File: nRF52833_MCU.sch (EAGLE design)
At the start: 44 parts, among them IC1 SKY13415-485LF, J1 282834-2, J100 DEBUG_CONNECTOR, J2 282834-2, J3 282834-2, U1 nRF52833-QIAA, U3 BQ25570RGRR, X1 32MHz, X2 32.768kHz, X3 22-23-2031

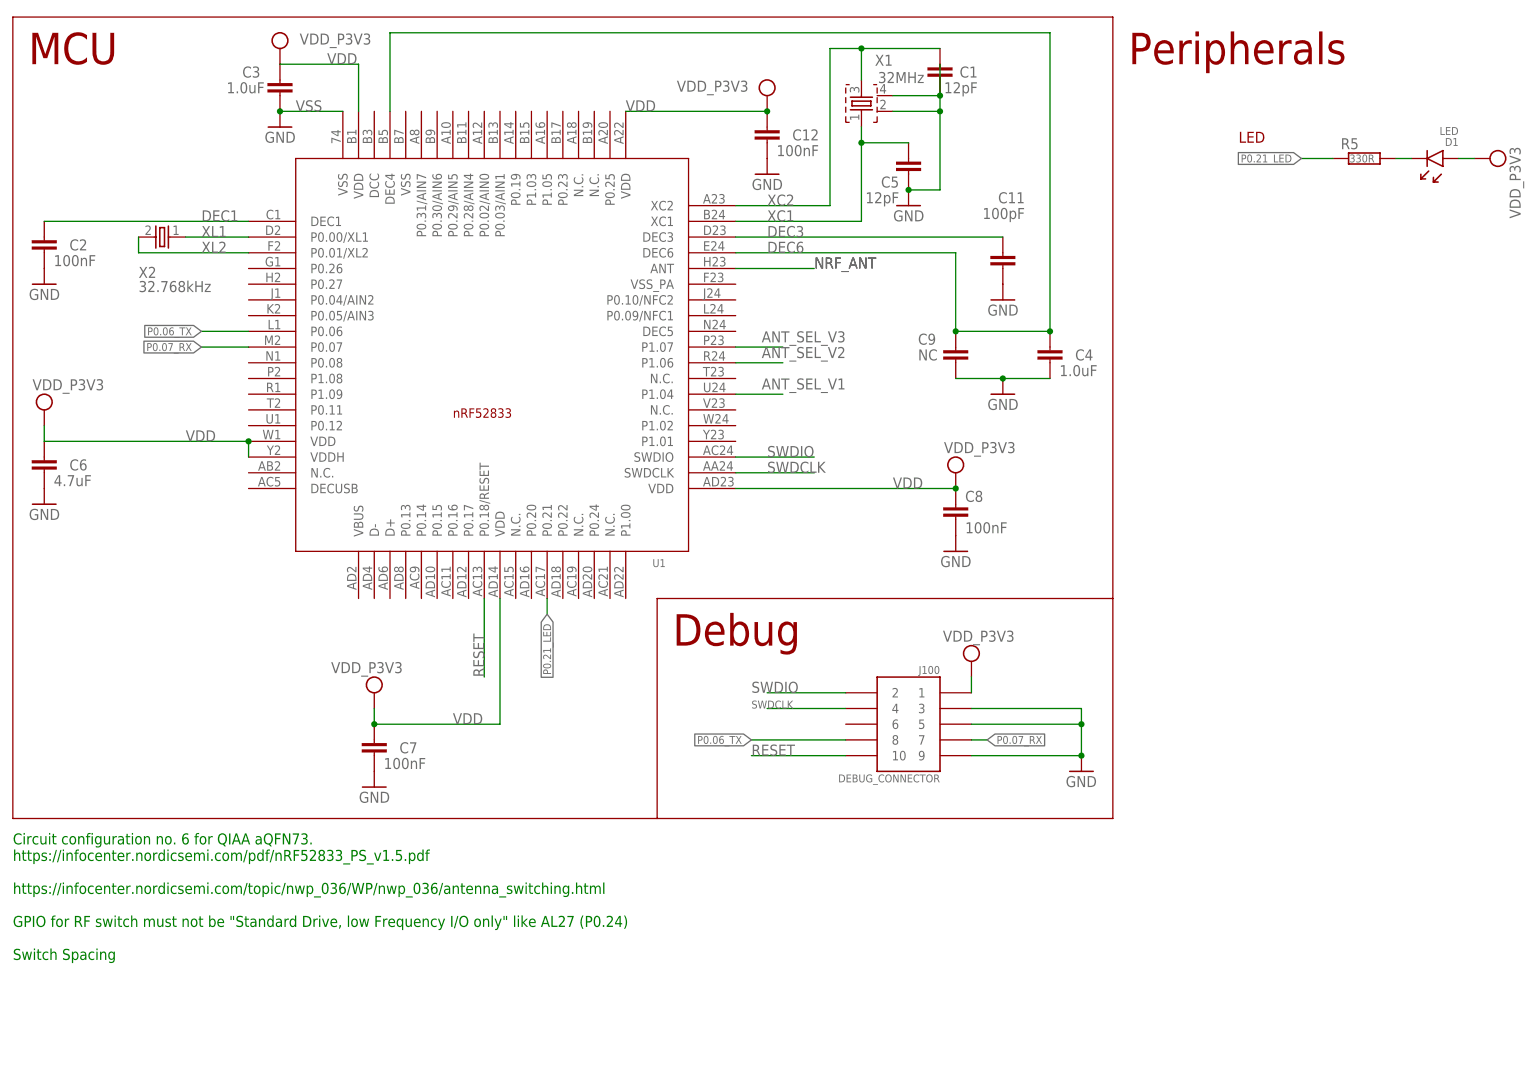
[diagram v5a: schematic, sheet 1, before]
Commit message: Add the 5 antennas
Signed-off-by: Florian Depraz <florian.depraz@outlook.com>
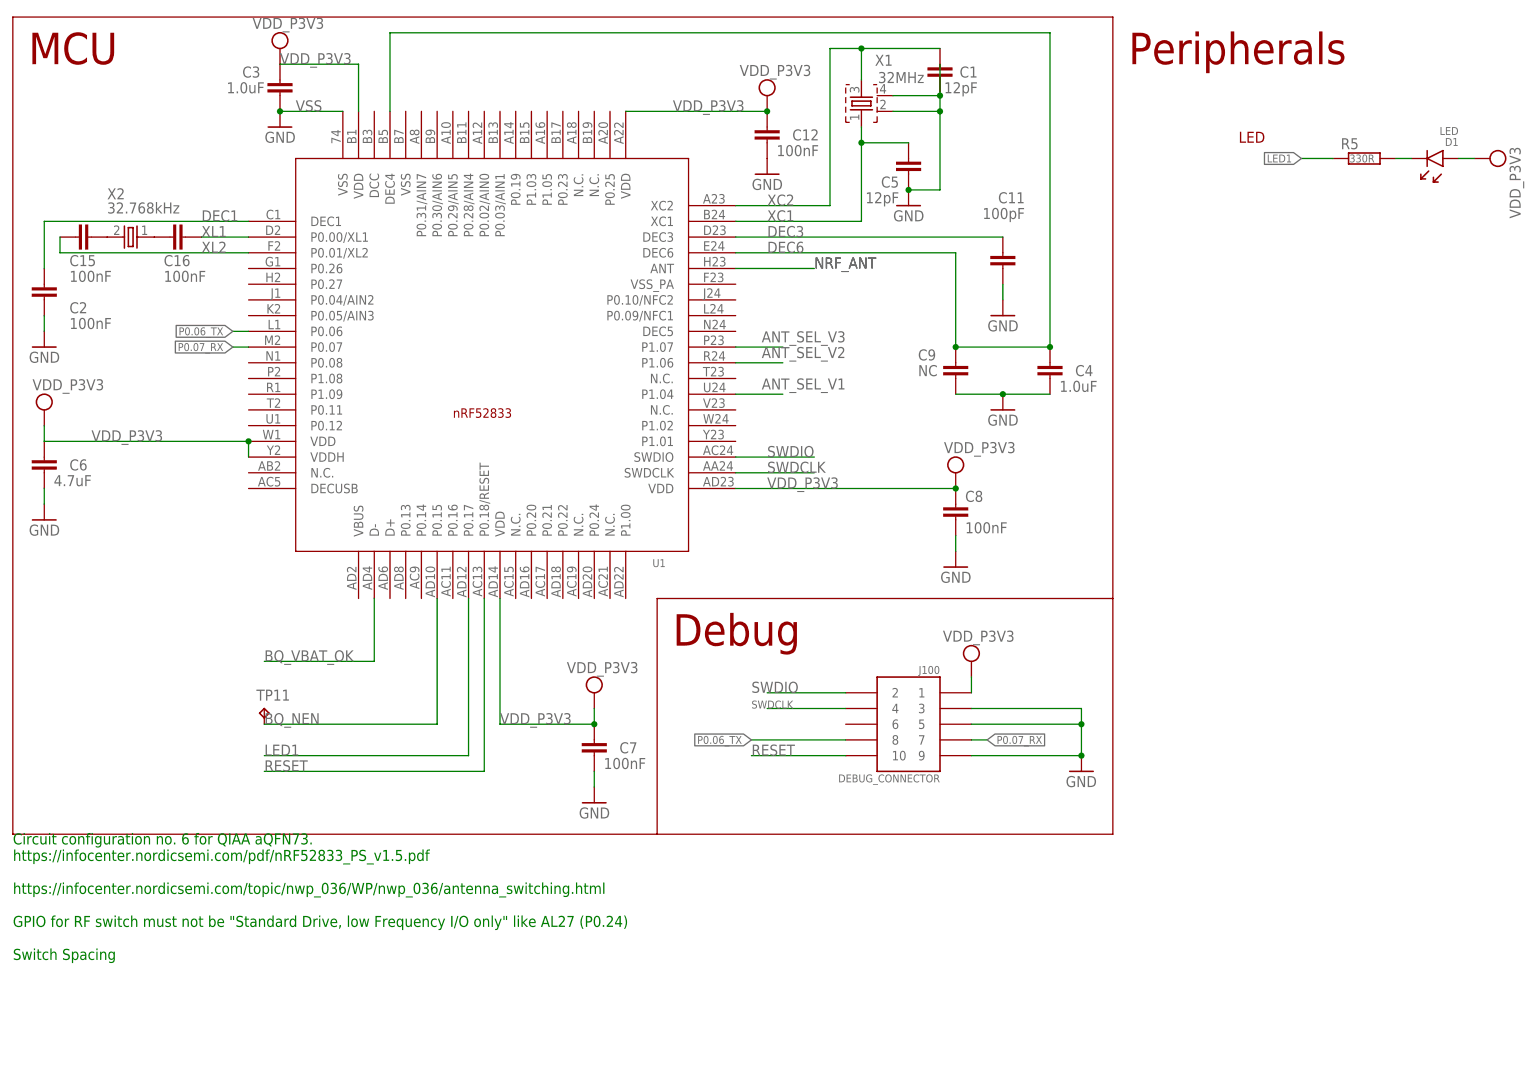
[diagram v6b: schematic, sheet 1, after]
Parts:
- added ANT3: (no value), discrete:ANTENNA
- added ANT4, ANT5: SWRA092B, texas:SWRA092B
- added C15, C16: 100nF, Nordic_misc:CAPACITOR_0402_N
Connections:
- removed net BQ_OK_HYST: U3.OK_HYST
- removed net BQ_OK_PROG: U3.OK_PROG
- removed net GND: C1.2, C10.2, C11.2, C12.2, C13.2, C14.2, C2.2, C20.2, C21.2, C23.2, C24.2, C25.2, C26.2, C27.2, C28.2, C29.2, C4.2, C5.2, C6.2, C7.2, C8.2, C9.2, J1.1, J100.3, J100.5, J100.9, J2.1, J3.1, U3.EP@1, U3.EP@2, U3.EP@3, U3.EP@4, U3.EP@5, U3.NC1, U3.NC2, U3.VSS@1, U3.VSS@2, X1.2, X1.4
- removed net P0.21_LED: R5.1, U1.P0.21
- removed net VDD: C12.1, C3.1, C6.1, C7.1, C8.1, U1.VDD@1, U1.VDD@2, U1.VDD@3, U1.VDD@4, U1.VDD@5, U1.VDDH
- new net LED1: R5.1, U1.P0.17
- new net N$2: C16.2, X2.1
- new net N$3: C15.2, X2.2
- net ANT_OUT_RF3: now also ANT4.ANTENNA
- net ANT_OUT_RF4: now also ANT3.1
- net ANT_OUT_RF5: now also ANT5.ANTENNA
- net BQ_NEN: now also TP11.TP, U1.P0.15
- net BQ_VBAT_OK: now also U1.D-
- net VDD_P3V3: now also C12.1, C3.1, C6.1, C7.1, C8.1, U1.VDD@1, U1.VDD@2, U1.VDD@3, U1.VDD@4, U1.VDD@5, U1.VDDH
- net VSS: now also C1.2, C10.2, C11.2, C12.2, C13.2, C14.2, C2.2, C20.2, C21.2, C23.2, C24.2, C25.2, C26.2, C27.2, C28.2, C29.2, C4.2, C5.2, C6.2, C7.2, C8.2, C9.2, J1.1, J100.3, J100.5, J100.9, J2.1, J3.1, U3.EP@1, U3.EP@2, U3.EP@3, U3.EP@4, U3.EP@5, U3.NC1, U3.NC2, U3.OK_HYST, U3.OK_PROG, U3.VSS@1, U3.VSS@2, X1.2, X1.4
- net XL1: now also C16.1; no longer X2.1
- net XL2: now also C15.1; no longer X2.2
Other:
- moved on the sheet: C2, C4, C7, C9, X2

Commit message: Fix errors
Signed-off-by: Florian Depraz <florian.depraz@outlook.com>
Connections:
- net VDD_P3V3 renamed VDD
- net VSS renamed GND
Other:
- moved on the sheet: C3, C6

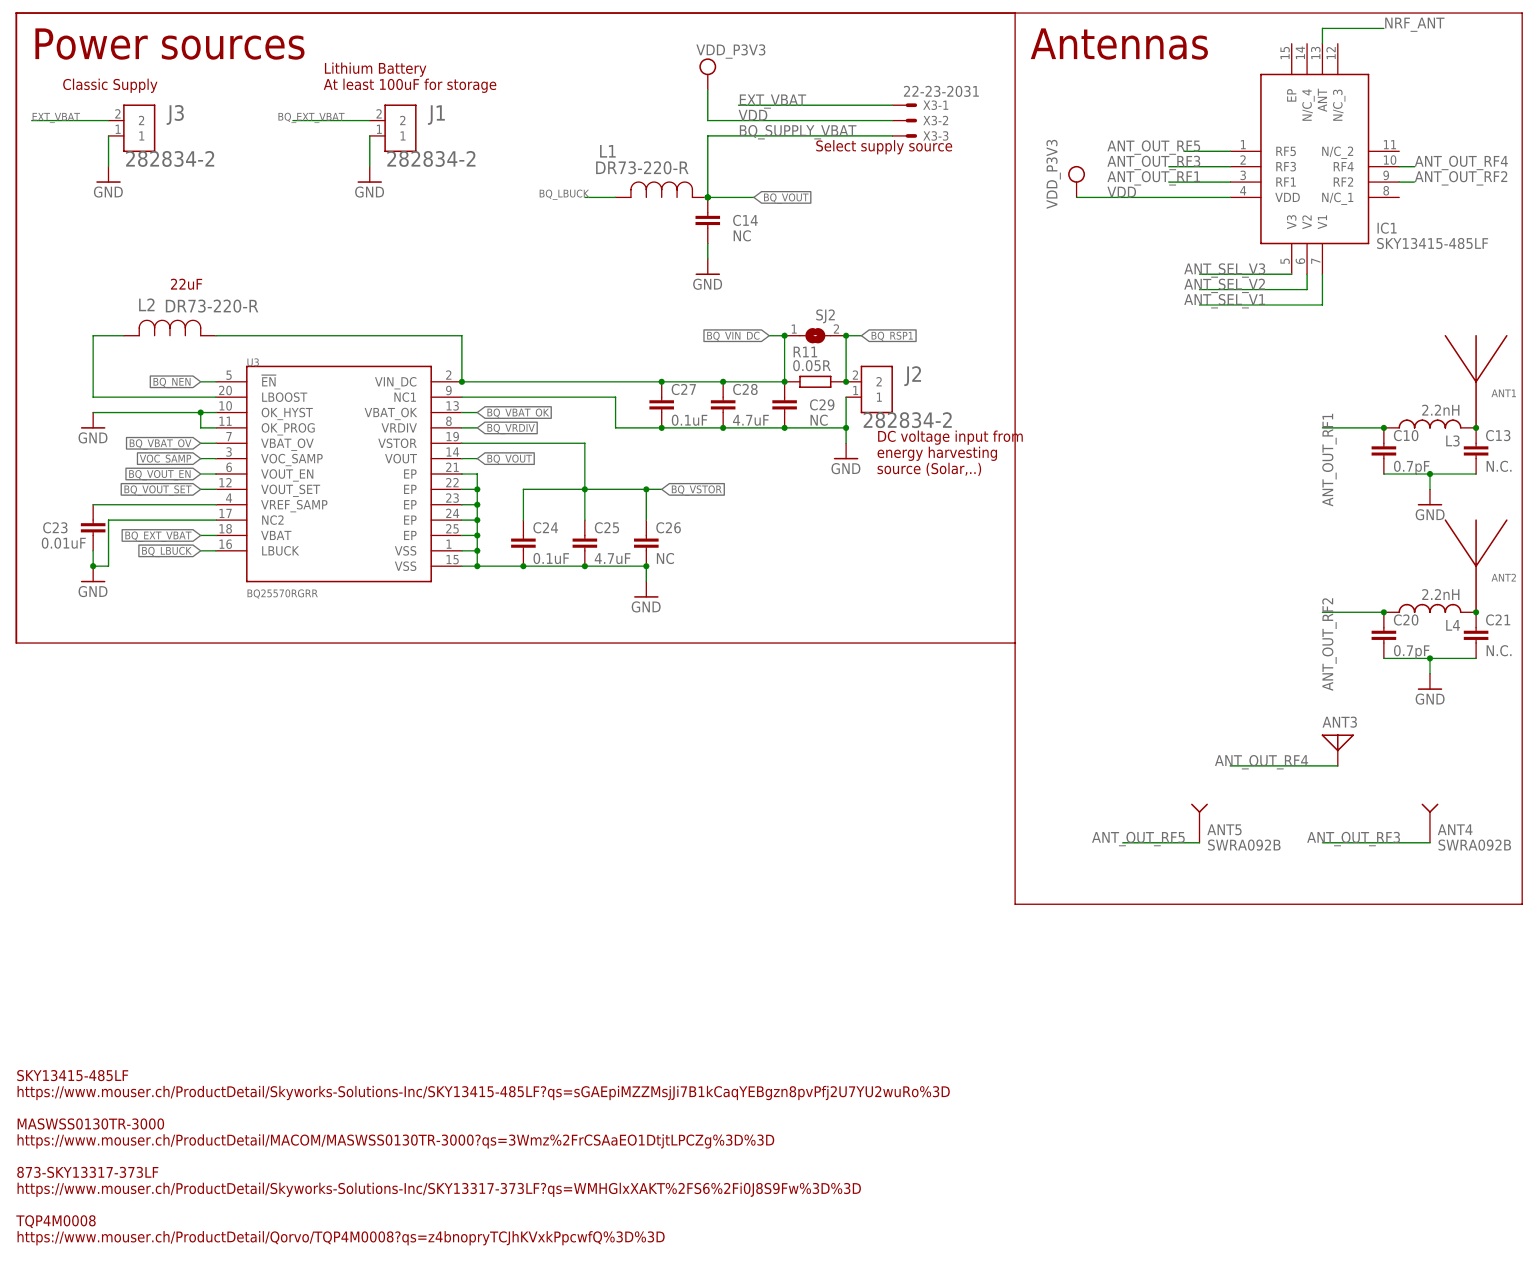
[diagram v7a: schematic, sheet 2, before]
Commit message: Routing the antennas
Signed-off-by: Florian Depraz <florian.depraz@outlook.com>
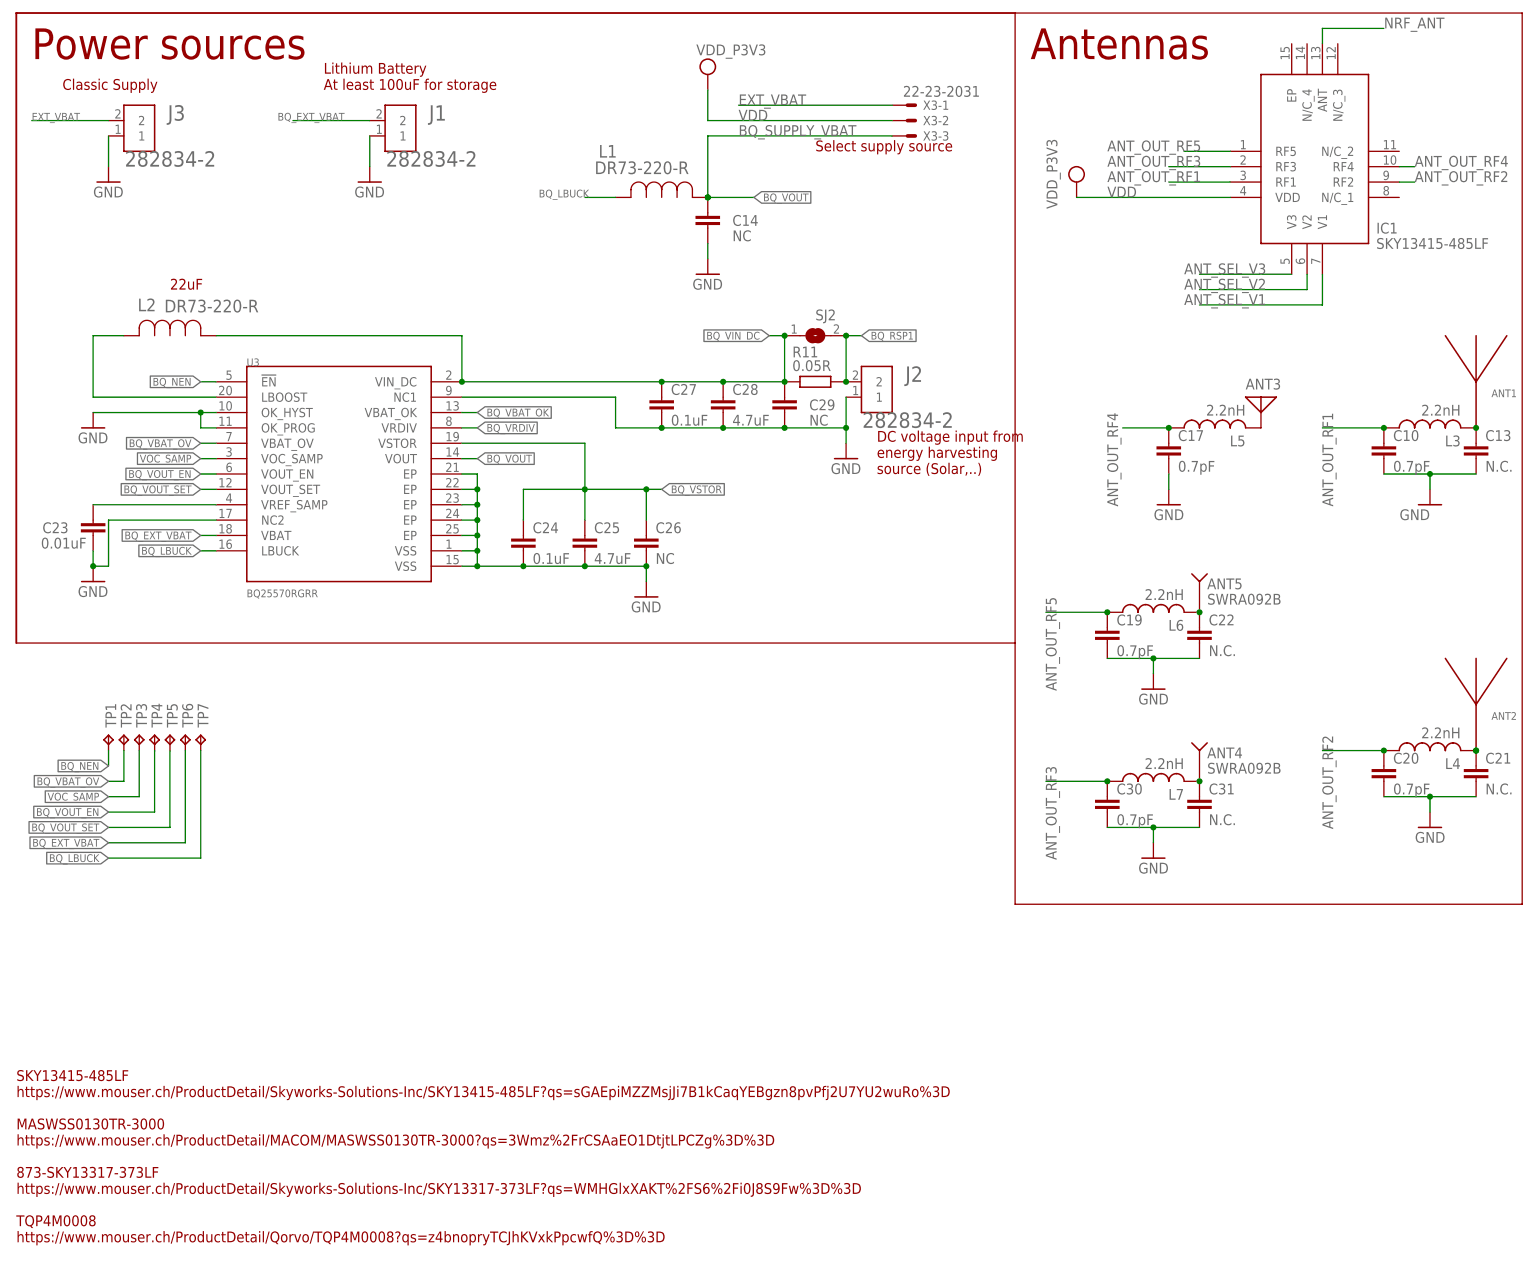
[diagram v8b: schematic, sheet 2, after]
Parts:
- added C17, C19, C30: 0.7pF, Nordic_misc:CAPACITOR_0402_N
- added C22, C31: N.C., Nordic_misc:CAPACITOR_0402_N
- added L5, L6, L7: 2.2nH, Nordic_misc:INDUCTOR_0402_N
- added TP1, TP2, TP3, TP4, TP5, TP6, TP7: TPPAD1-13, testpad:TPPAD1-13
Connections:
- new net N$12: ANT3.1, L5.2
- new net N$13: ANT5.ANTENNA, C22.1, L6.2
- new net N$14: ANT4.ANTENNA, C31.1, L7.2
- new net N$18: TP1.TP
- net ANT_OUT_RF3: now also C30.1, L7.1; no longer ANT4.ANTENNA
- net ANT_OUT_RF4: now also C17.1, L5.1; no longer ANT3.1
- net ANT_OUT_RF5: now also C19.1, L6.1; no longer ANT5.ANTENNA
- net BQ_EXT_VBAT: now also TP6.TP
- net BQ_LBUCK: now also TP7.TP
- net BQ_VBAT_OV: now also TP2.TP
- net BQ_VOUT_EN: now also TP4.TP
- net BQ_VOUT_SET: now also TP5.TP
- net GND: now also C17.2, C19.2, C22.2, C30.2, C31.2
- net VOC_SAMP: now also TP3.TP
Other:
- moved on the sheet: ANT2, ANT3, ANT4, ANT5, C20, C21, C3, L4
